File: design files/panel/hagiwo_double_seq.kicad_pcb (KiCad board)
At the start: 2 copper layers, 29.9 x 128.4 mm, 6 parts

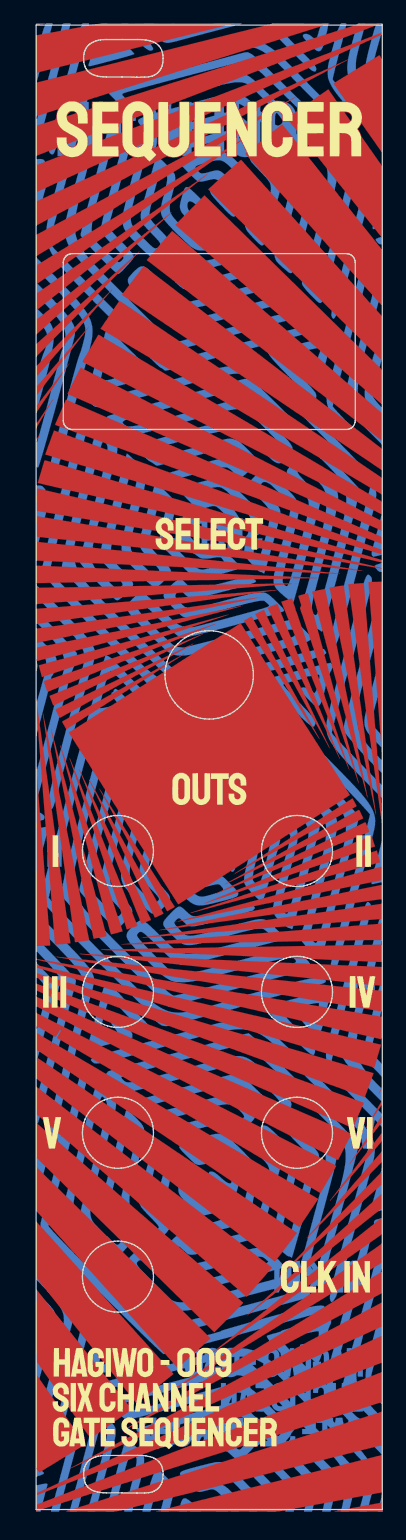
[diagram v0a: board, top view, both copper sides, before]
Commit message: new symmetric pcb and panel
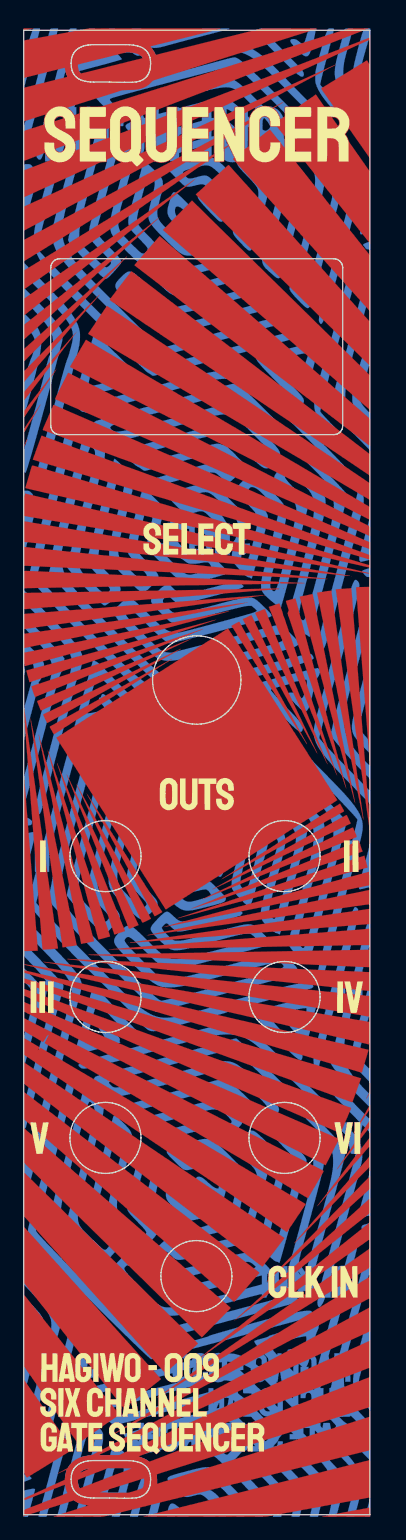
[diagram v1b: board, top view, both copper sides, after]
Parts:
- removed the G*** at (16.6, 64.9) (x6)
- added G*** (x6): LOGO, LOGO, F.Cu at (15.6, 65.3)
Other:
- outline, holes or cut-outs redrawn
